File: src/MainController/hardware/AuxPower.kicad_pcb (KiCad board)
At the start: 2 copper layers, 90 x 90 mm, 128 parts, among them J1 MC 1,5/2, J10 MC 1,5/4, J11 S3B-XH-A, J12 S3B-XH-A, J13 S3B-XH-A, J14 S3B-XH-A, J15 S3B-XH-A, J16 B3B-XH-A, J17 B4B-XH-A, J2 MC 1,5/2, J3 MC 1,5/2, J4 MC 1,5/2, J5 MC 1,5/2, J6 MC 1,5/4, J7 MC 1,5/4, J8 MC 1,5/4, J9 MC 1,5/4, Q1 BC846B,235, Q10 AO4421, Q2 BC846B,235, Q3 BC846B,235, Q4 BC846B,235, Q5 BC846B,235, Q6 AO4421, Q7 AO4421, Q8 AO4421, Q9 AO4421, U1 ZXCT1009, U2 ZXCT1009, U3 ZXCT1009, U5 ZXCT1009, U6 PIC18F26K83, U7 PI4IOE5V6416, U8 MCP9701

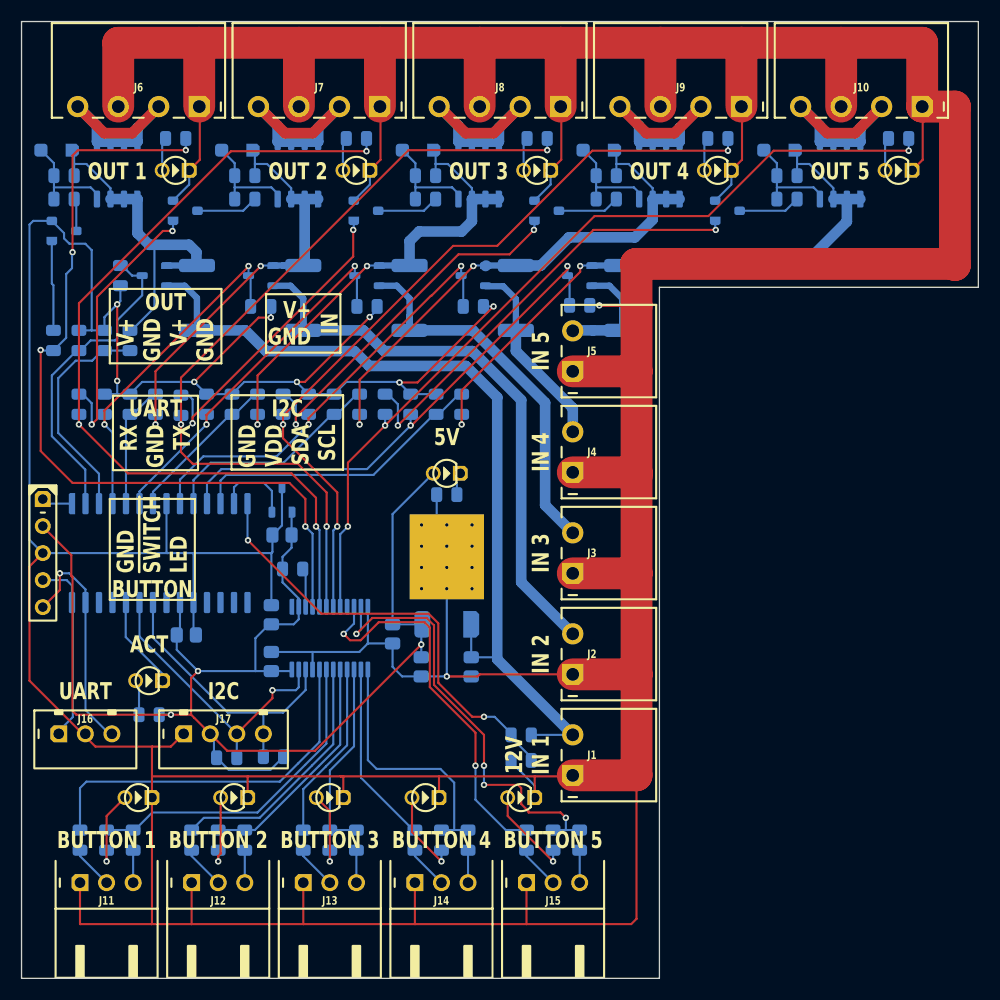
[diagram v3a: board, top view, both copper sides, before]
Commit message: MainController: making output open-drain
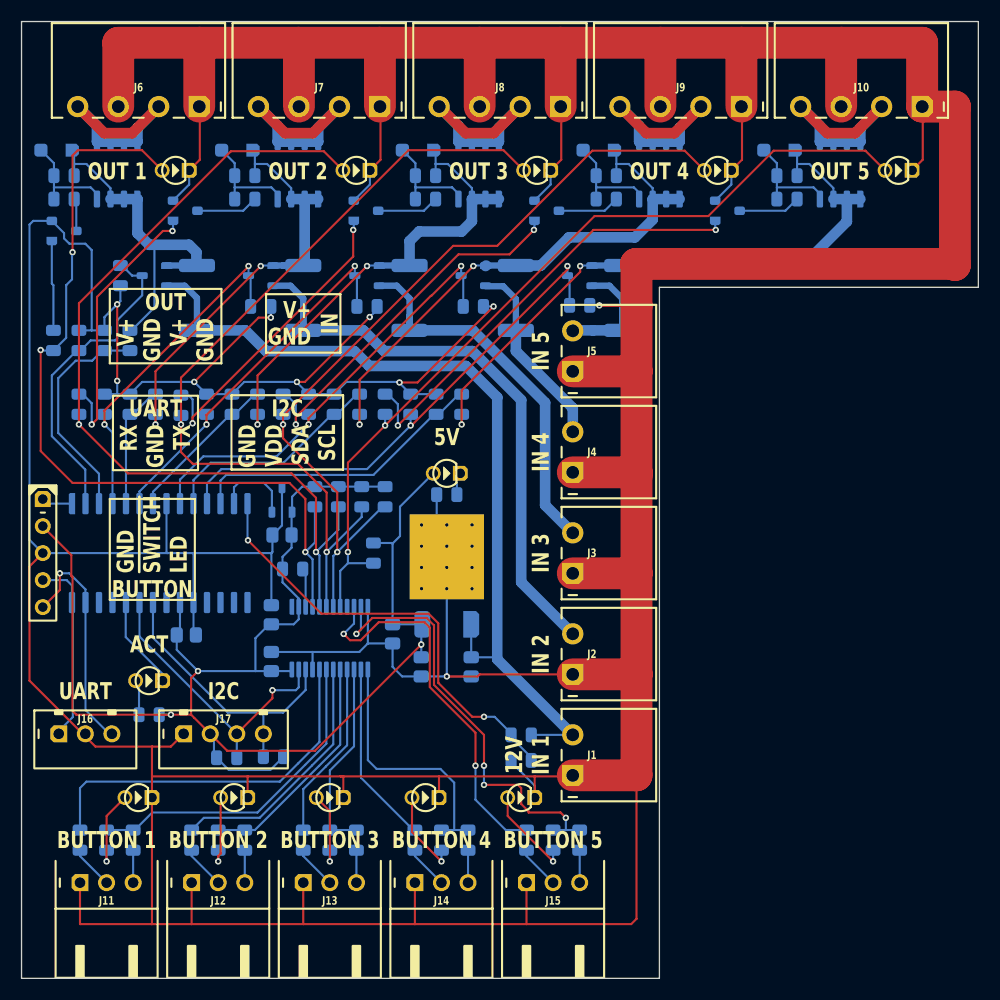
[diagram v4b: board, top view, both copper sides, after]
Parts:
- moved R25 62.9 mm to (48.1, 65.0), turned to -90 degrees
- moved R24 46.0 mm to (49.2, 59.7), turned to -90 degrees
- moved R23 37.5 mm to (47.0, 59.7), turned to -90 degrees
- moved R21 36.2 mm to (42.6, 59.7), turned to -90 degrees
- moved R22 33.7 mm to (44.8, 59.7), turned to -90 degrees
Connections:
- DS10 pad 2: LED_OUT_5 -> OUT_OUTPUT5
- DS6 pad 2: LED_OUT_1 -> OUT_OUTPUT1
- DS7 pad 2: LED_OUT_2 -> OUT_OUTPUT2
- DS8 pad 2: LED_OUT_3 -> OUT_OUTPUT3
- DS9 pad 2: LED_OUT_4 -> OUT_OUTPUT4
- R21 pad 1: LED_OUT_1 -> 5V
- R22 pad 1: LED_OUT_2 -> 5V
- R23 pad 1: LED_OUT_3 -> 5V
- R24 pad 1: LED_OUT_4 -> 5V
- R25 pad 1: LED_OUT_5 -> 5V
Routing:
- net 5V: track 127.6 -> 140.0 mm
- net OUT_OUTPUT4: track 74.5 -> 78.2 mm, vias 3 -> 2
- net OUT_OUTPUT3: track 78.3 -> 81.4 mm, vias 3 -> 2
- net LED_OUT_5: track 2.68 -> 0.00 mm
- net LED_OUT_4: track 2.68 -> 0.00 mm
- net LED_OUT_3: track 2.68 -> 0.00 mm
- net LED_OUT_2: track 2.68 -> 0.00 mm
- net LED_OUT_1: track 2.68 -> 0.00 mm
- net OUT_OUTPUT2: track 82.1 -> 84.5 mm, vias 3 -> 2
- net OUT_OUTPUT1: track 79.0 -> 81.1 mm, vias 4 -> 3
- net OUT_OUTPUT5: track 81.0 -> 80.8 mm, vias 3 -> 2

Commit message: MainController: Changed transistor base resistor to 10K
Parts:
- R47: renamed from R11; value 1K -> 10K
- R48: renamed from R12; value 1K -> 10K
- R49: renamed from R13; value 1K -> 10K
- R50: renamed from R14; value 1K -> 10K
- R51: renamed from R15; value 1K -> 10K
- renumbered R16 to R11, R17 to R12, R18 to R13, R19 to R14, R20 to R15, R21 to R16, R22 to R17, R23 to R18, R24 to R19, R25 to R20, R26 to R21, R27 to R22, R28 to R23, R29 to R24, R30 to R25, R31 to R26, R32 to R27, R33 to R28, R34 to R29, R35 to R30, R36 to R31, R37 to R32, R38 to R33, R39 to R34, R40 to R35, R41 to R36, R42 to R37, R43 to R38, R44 to R39, R45 to R40, R46 to R41, R47 to R42, R48 to R43, R49 to R44, R50 to R45, R51 to R46
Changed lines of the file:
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@@
 		(at 57.5 41.8)
 		(tags "RESC2013X70N")
-		(property "Reference" "R35"
+		(property "Reference" "R30"
 			(at 0 1.6 0)
 			(layer "B.SilkS")
@@
 		(at 48.1 65 -90)
 		(tags "RESC2013X70N")
-		(property "Reference" "R25"
+		(property "Reference" "R20"
 			(at 0 1.6 90)
 			(layer "B.SilkS")
@@
 		(at 34.8 51 90)
 		(tags "RESC2013X70N")
-		(property "Reference" "R49"
+		(property "Reference" "R44"
 			(at 0 1.6 90)
 			(layer "B.SilkS")
@@
 		(at 67.5 41.7)
 		(tags "RESC2013X70N")
-		(property "Reference" "R34"
+		(property "Reference" "R29"
 			(at 0 1.6 0)
 			(layer "B.SilkS")
@@
 		(at 32.4 51 90)
 		(tags "RESC2013X70N")
-		(property "Reference" "R18"
+		(property "Reference" "R13"
 			(at 0 1.6 90)
 			(layer "B.SilkS")
@@
 		(at 18 45 -90)
 		(tags "RESC2013X70N")
-		(property "Reference" "R11"
+		(property "Reference" "R47"
 			(at 0 1.6 90)
 			(layer "B.SilkS")
@@
 			)
 		)
-		(property "Value" "1K"
+		(property "Value" "10K"
 			(at -2.3 0 0)
 			(layer "B.SilkS")
@@
 		(at 20.4 51 90)
 		(tags "RESC2013X70N")
-		(property "Reference" "R12"
+		(property "Reference" "R48"
 			(at 0 1.6 90)
 			(layer "B.SilkS")
@@
 			)
 		)
-		(property "Value" "1K"
+		(property "Value" "10K"
 			(at 2.3 0 0)
 			(layer "B.SilkS")
@@
 		(at 23 92 90)
 		(tags "RESC2013X70N")
-		(property "Reference" "R26"
+		(property "Reference" "R21"
 			(at 0 1.6 90)
 			(layer "B.SilkS")
@@
 		(at 42.6 59.7 -90)
 		(tags "RESC2013X70N")
-		(property "Reference" "R21"
+		(property "Reference" "R16"
 			(at 0 1.6 90)
 			(layer "B.SilkS")
@@
 		(at 20.4 45 90)
 		(tags "RESC2013X70N")
-		(property "Reference" "R16"
+		(property "Reference" "R11"
 			(at 0 1.6 90)
 			(layer "B.SilkS")
@@
 		(at 49.2 59.7 -90)
 		(tags "RESC2013X70N")
-		(property "Reference" "R24"
+		(property "Reference" "R19"
 			(at 0 1.6 90)
 			(layer "B.SilkS")
@@
 		(at 51.6 51 90)
 		(tags "RESC2013X70N")
-		(property "Reference" "R20"
+		(property "Reference" "R15"
 			(at 0 1.6 90)
 			(layer "B.SilkS")
@@
 		(at 47.5 41.8)
 		(tags "RESC2013X70N")
-		(property "Reference" "R36"
+		(property "Reference" "R31"
 			(at 0 1.6 0)
 			(layer "B.SilkS")
@@
 		(at 44.4 51 90)
 		(tags "RESC2013X70N")
-		(property "Reference" "R50"
+		(property "Reference" "R45"
 			(at 0 1.6 90)
 			(layer "B.SilkS")
@@
 		(at 42 51 90)
 		(tags "RESC2013X70N")
-		(property "Reference" "R19"
+		(property "Reference" "R14"
 			(at 0 1.6 90)
 			(layer "B.SilkS")
@@
 		(at 40.5 66.5 180)
 		(tags "RESC2013X70N")
-		(property "Reference" "R33"
+		(property "Reference" "R28"
 			(at 0 1.6 0)
 			(layer "B.SilkS")
@@
 		(at 44.8 59.7 -90)
 		(tags "RESC2013X70N")
-		(property "Reference" "R22"
+		(property "Reference" "R17"
 			(at 0 1.6 90)
 			(layer "B.SilkS")
@@
 		(at 44 92 90)
 		(tags "RESC2013X70N")
-		(property "Reference" "R28"
+		(property "Reference" "R23"
 			(at 0 1.6 90)
 			(layer "B.SilkS")
@@
 		(at 33.5 92 90)
 		(tags "RESC2013X70N")
-		(property "Reference" "R27"
+		(property "Reference" "R22"
 			(at 0 1.6 90)
 			(layer "B.SilkS")
@@
 		(at 20.5 92 90)
 		(tags "RESC2013X70N")
-		(property "Reference" "R40"
+		(property "Reference" "R35"
 			(at 0 1.6 90)
 			(layer "B.SilkS")
@@
 		(at 38.7 84.15)
 		(tags "RESC2013X70N")
-		(property "Reference" "R46"
+		(property "Reference" "R41"
 			(at 0 1.6 0)
 			(layer "B.SilkS")
@@
 		(at 34.3 84.25 180)
 		(tags "RESC2013X70N")
-		(property "Reference" "R45"
+		(property "Reference" "R40"
 			(at 0 1.6 0)
 			(layer "B.SilkS")
@@
 		(at 65 92 90)
 		(tags "RESC2013X70N")
-		(property "Reference" "R30"
+		(property "Reference" "R25"
 			(at 0 1.6 90)
 			(layer "B.SilkS")
@@
 		(at 37.5 41.8)
 		(tags "RESC2013X70N")
-		(property "Reference" "R37"
+		(property "Reference" "R32"
 			(at 0 1.6 0)
 			(layer "B.SilkS")
@@
 		(at 47 59.7 -90)
 		(tags "RESC2013X70N")
-		(property "Reference" "R23"
+		(property "Reference" "R18"
 			(at 0 1.6 90)
 			(layer "B.SilkS")
@@
 		(at 27 80.2)
 		(tags "RESC2013X70N")
-		(property "Reference" "R32"
+		(property "Reference" "R27"
 			(at 0 1.6 0)
 			(layer "B.SilkS")
@@
 		(at 54 51 90)
 		(tags "RESC2013X70N")
-		(property "Reference" "R51"
+		(property "Reference" "R46"
 			(at 0 1.6 90)
 			(layer "B.SilkS")
@@
 		(at 52 92 90)
 		(tags "RESC2013X70N")
-		(property "Reference" "R43"
+		(property "Reference" "R38"
 			(at 0 1.6 90)
 			(layer "B.SilkS")
@@
 		(at 30 51.1 90)
 		(tags "RESC2013X70N")
-		(property "Reference" "R13"
+		(property "Reference" "R49"
 			(at 0 1.6 90)
 			(layer "B.SilkS")
@@
 			)
 		)
-		(property "Value" "1K"
+		(property "Value" "10K"
 			(at 2.3 0 180)
 			(layer "B.SilkS")
@@
 		(at 31 92 90)
 		(tags "RESC2013X70N")
-		(property "Reference" "R41"
+		(property "Reference" "R36"
 			(at 0 1.6 90)
 			(layer "B.SilkS")
@@
 		(at 22.8 45 90)
 		(tags "RESC2013X70N")
-		(property "Reference" "R47"
+		(property "Reference" "R42"
 			(at 0 1.6 90)
 			(layer "B.SilkS")
@@
 		(at 39.6 51 90)
 		(tags "RESC2013X70N")
-		(property "Reference" "R14"
+		(property "Reference" "R50"
 			(at 0 1.6 90)
 			(layer "B.SilkS")
@@
 			)
 		)
-		(property "Value" "1K"
+		(property "Value" "10K"
 			(at 2.3 0 180)
 			(layer "B.SilkS")
@@
 		(at 49.2 51 90)
 		(tags "RESC2013X70N")
-		(property "Reference" "R15"
+		(property "Reference" "R51"
 			(at 0 1.6 90)
 			(layer "B.SilkS")
@@
 			)
 		)
-		(property "Value" "1K"
+		(property "Value" "10K"
 			(at 2.3 0 180)
 			(layer "B.SilkS")
@@
 		(at 22.8 51 90)
 		(tags "RESC2013X70N")
-		(property "Reference" "R17"
+		(property "Reference" "R12"
 			(at 0 1.6 90)
 			(layer "B.SilkS")
@@
 		(at 24.3 38.9 -90)
 		(tags "RESC2013X70N")
-		(property "Reference" "R38"
+		(property "Reference" "R33"
 			(at 0 1.6 90)
 			(layer "B.SilkS")
@@
 		(at 41.5 92 90)
 		(tags "RESC2013X70N")
-		(property "Reference" "R42"
+		(property "Reference" "R37"
 			(at 0 1.6 90)
 			(layer "B.SilkS")
@@
 		(at 55 59.5)
 		(tags "RESC2013X70N")
-		(property "Reference" "R31"
+		(property "Reference" "R26"
 			(at 0 1.6 0)
 			(layer "B.SilkS")
@@
 		(at 62 84.5 180)
 		(tags "RESC2013X70N")
-		(property "Reference" "R39"
+		(property "Reference" "R34"
 			(at 0 1.6 0)
 			(layer "B.SilkS")
@@
 		(at 62.5 92 90)
 		(tags "RESC2013X70N")
-		(property "Reference" "R44"
+		(property "Reference" "R39"
 			(at 0 1.6 90)
 			(layer "B.SilkS")
@@
 		(at 54.5 92 90)
 		(tags "RESC2013X70N")
-		(property "Reference" "R29"
+		(property "Reference" "R24"
 			(at 0 1.6 90)
 			(layer "B.SilkS")
@@
 		(at 25.2 51 90)
 		(tags "RESC2013X70N")
-		(property "Reference" "R48"
+		(property "Reference" "R43"
 			(at 0 1.6 90)
 			(layer "B.SilkS")
@@
 		(width 0.2)
 		(layer "B.Cu")
-		(net 22)
-	)
-	(segment
-		(start 48.95 60.65)
-		(end 49.2 60.65)
-		(width 0.2)
-		(layer "B.Cu")

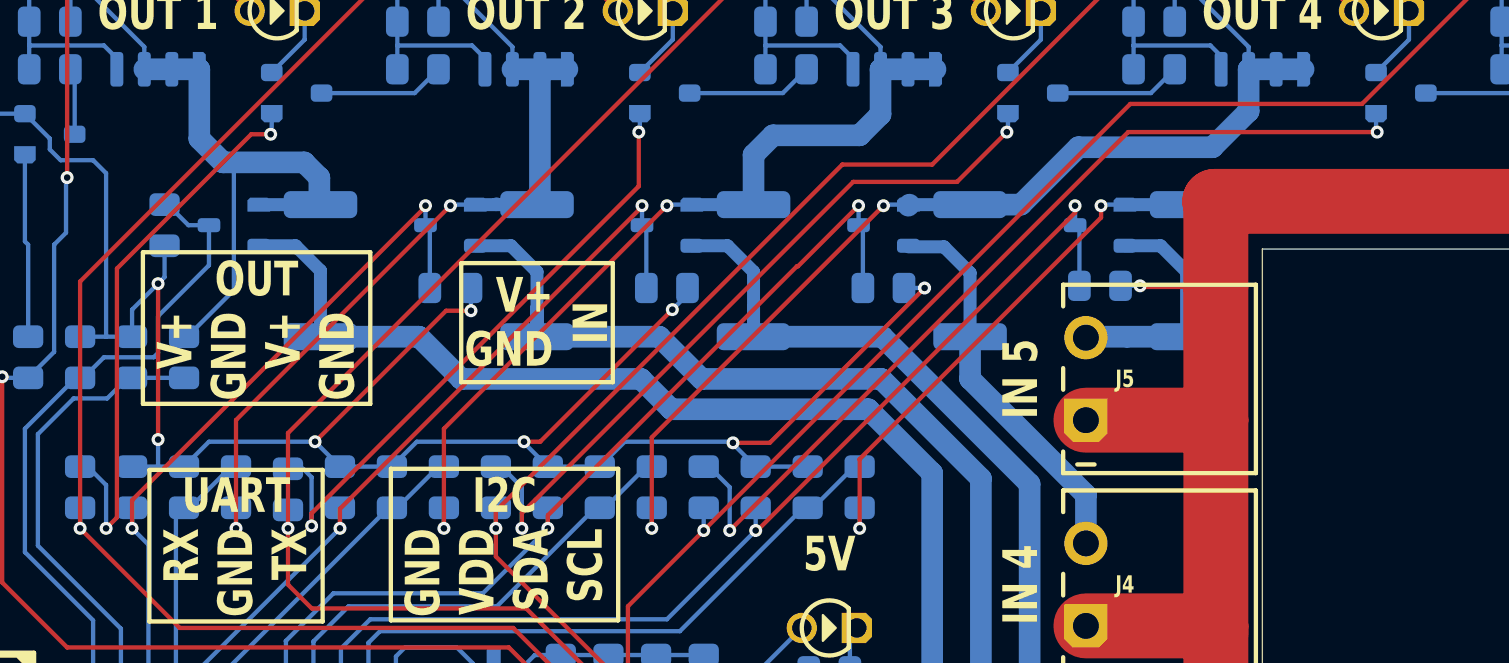
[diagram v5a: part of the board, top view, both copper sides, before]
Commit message: MainController: Changed ZXCT1009 to HV7801
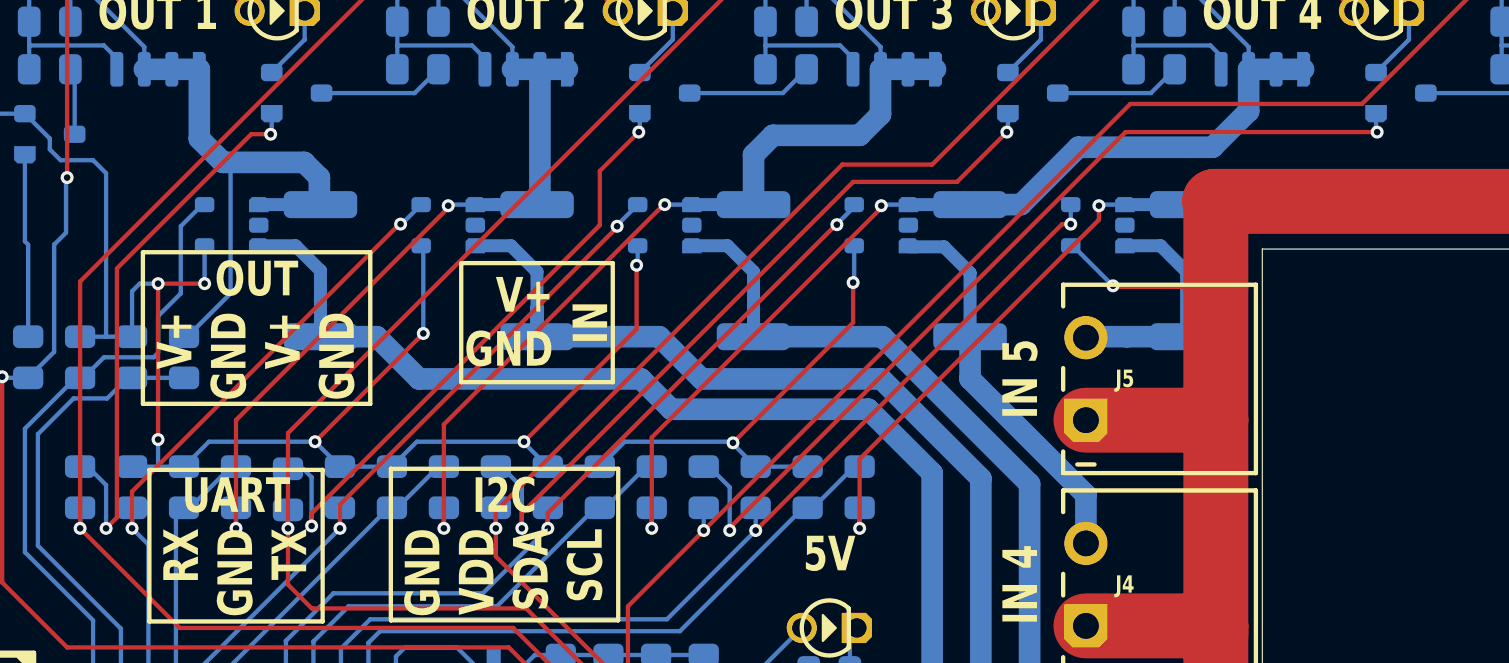
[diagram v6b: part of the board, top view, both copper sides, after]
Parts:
- removed the R29 at (67.5, 41.7)
- removed the R30 at (57.5, 41.8)
- removed the R31 at (47.5, 41.8)
- removed the R32 at (37.5, 41.8)
- removed the R33 at (24.3, 38.9)
- U1, U2, U3, U5 (x2): footprint Medo64:U Current Monitor [ZXCT1009] (SOT23-3) -> Medo64:U CurrentMonitor [HV7801] (SOT23-5)
- moved U1 0.10 mm to (27.4, 38.9), turned to 180 degrees
- moved U2 0.10 mm to (37.4, 38.9), turned to 180 degrees
- moved U3 0.10 mm to (47.4, 38.9), turned to 180 degrees
- moved U5 0.10 mm to (57.4, 38.9), turned to 180 degrees
- moved U5 0.10 mm to (67.4, 38.9), turned to 180 degrees
- renumbered R34 to R29, R35 to R30, R36 to R31, R37 to R32, R38 to R33, R39 to R34, R40 to R35, R41 to R36, R42 to R37, R43 to R38, R44 to R39, R45 to R40, R46 to R41, R47 to R42, R48 to R43, R49 to R44, R50 to R45, R51 to R46, R52 to R47, R53 to R48, R54 to R49, R55 to R50, R56 to R51, R57 to R52, R58 to R53, R59 to R54, R60 to R55, R61 to R56, R62 to R57, R63 to R58, R64 to R59, R65 to R60, R66 to R61, R67 to R62
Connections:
- U1 pad 2: INPUT1 -> (no net)
- U1 pad 3: ADC_CURRENT1 -> INPUT1
- U2 pad 2: INPUT2 -> (no net)
- U2 pad 3: ADC_CURRENT2 -> INPUT2
- U3 pad 2: INPUT3 -> (no net)
- U3 pad 3: ADC_CURRENT3 -> INPUT3
- U5 pad 2: INPUT4 -> (no net)
- U5 pad 3: ADC_CURRENT4 -> INPUT4
- U5 pad 2: INPUT5 -> (no net)
- U5 pad 3: ADC_CURRENT5 -> INPUT5
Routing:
- net GND: track 749.1 -> 754.6 mm, vias 10 -> 11
- net ADC_CURRENT4: track 41.9 -> 38.2 mm
- net ADC_CURRENT3: track 35.3 -> 31.7 mm
- net ADC_CURRENT2: track 32.8 -> 29.3 mm
- net ADC_CURRENT5: track 49.1 -> 45.8 mm
- net ADC_CURRENT1: track 29.8 -> 28.3 mm
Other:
- board text added: "AuxPower BXXXX"
- board text removed: "AuxPower AXXXX"

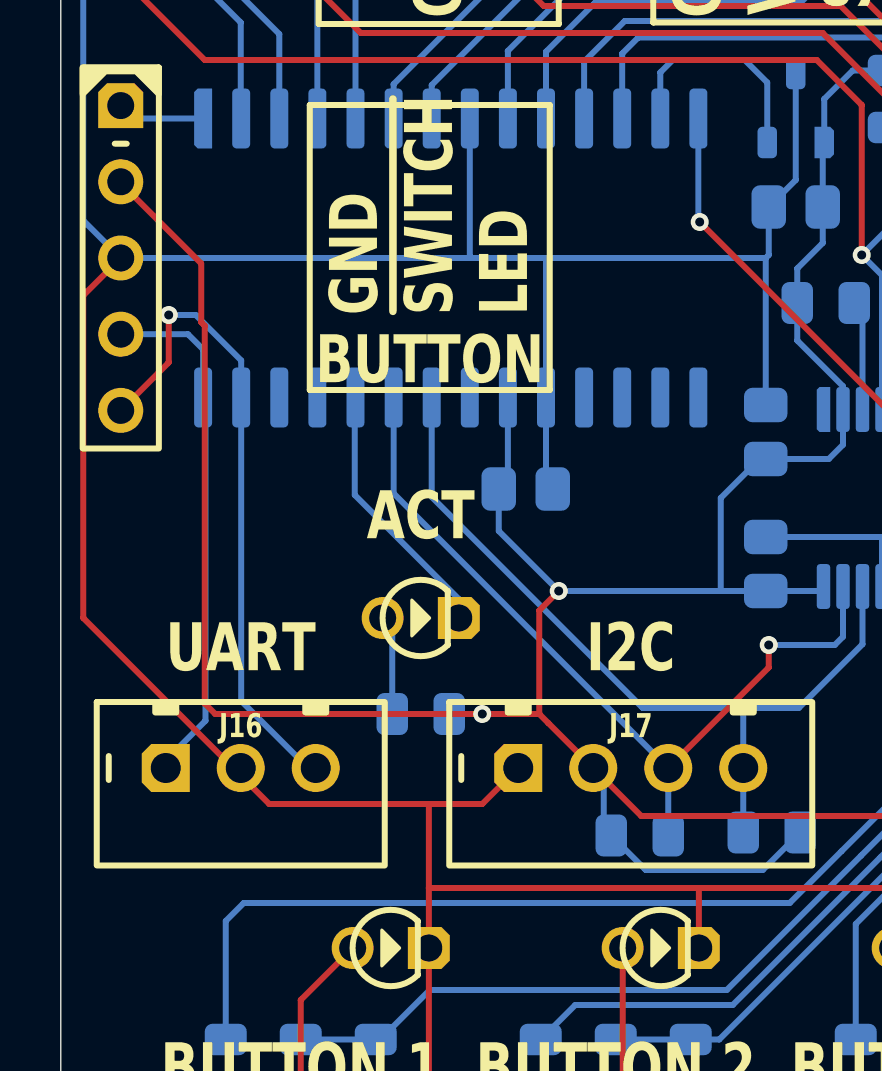
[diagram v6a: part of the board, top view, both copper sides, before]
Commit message: MainController: moved UART lines
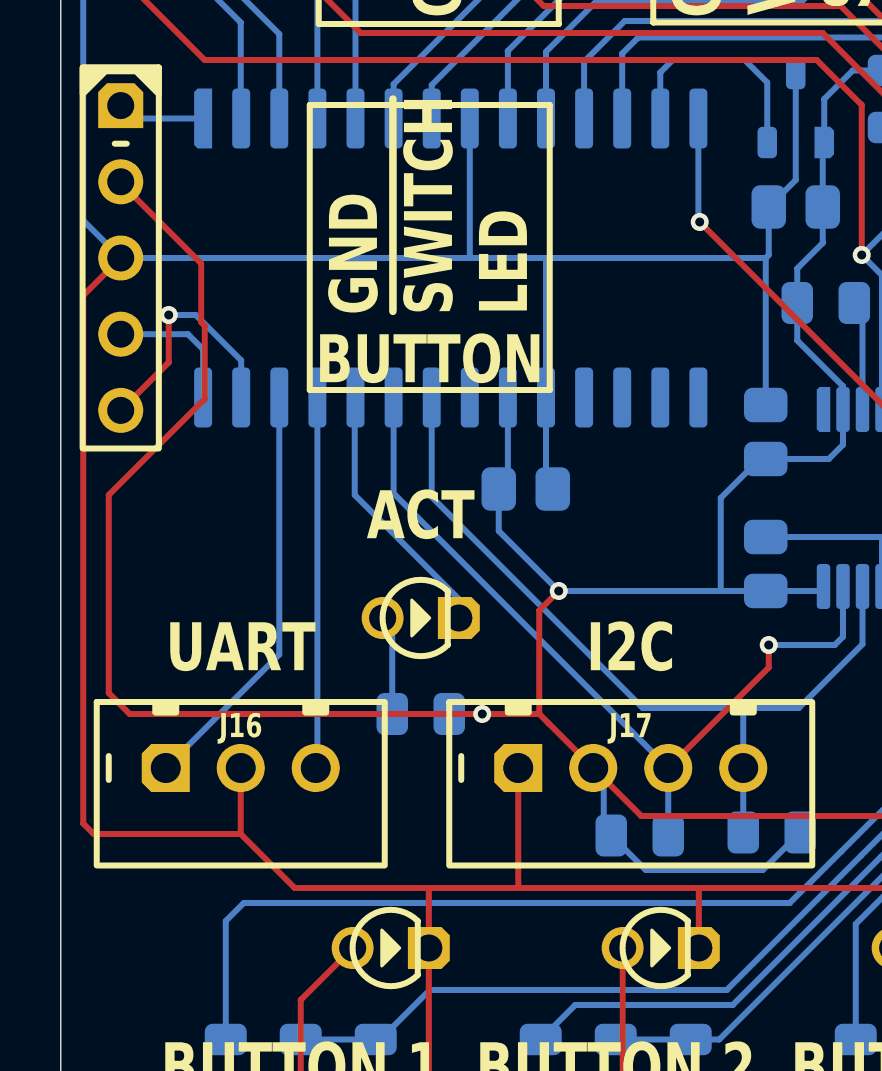
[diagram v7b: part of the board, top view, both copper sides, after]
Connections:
- ICSP pad 4: UART_RX ICSP_DAT -> ICSP_DAT
- ICSP pad 5: UART_TX ICSP_CLK -> ICSP_CLK
- J16 pad 1: UART_RX ICSP_DAT -> UART_RX
- J16 pad 3: UART_TX ICSP_CLK -> UART_TX
- U6 pad 25: (no net) -> UART_TX
- U6 pad 26: (no net) -> UART_RX
- U6 pad 27: UART_TX ICSP_CLK -> ICSP_CLK
- U6 pad 28: UART_RX ICSP_DAT -> ICSP_DAT
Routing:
- net UART_TX ICSP_CLK: track 21.8 -> 0.00 mm, vias 1 -> 0
- net UART_RX ICSP_DAT: track 17.7 -> 0.00 mm
- net UART_RX: track 0.00 -> 13.9 mm
- net UART_TX: track 0.00 -> 12.4 mm
- net ICSP_CLK: track 0.00 -> 8.12 mm, vias 0 -> 1
- net GND: track 754.6 -> 759.7 mm
- net ICSP_DAT: track 0.00 -> 4.56 mm
- net 5V: track 140.0 -> 144.3 mm
